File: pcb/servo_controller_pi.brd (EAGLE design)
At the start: 129 parts, among them IC1 PIC18F452, IC2 DS1307, IC3 MAX4173FESA+, IC4 LM2936MP-3.3, IC6 LM386M-1, IC7 GY-27, IC8 MCP23017SO, Q1 10Mhz, Q2 BC848ASMD, Q3 BC848ASMD

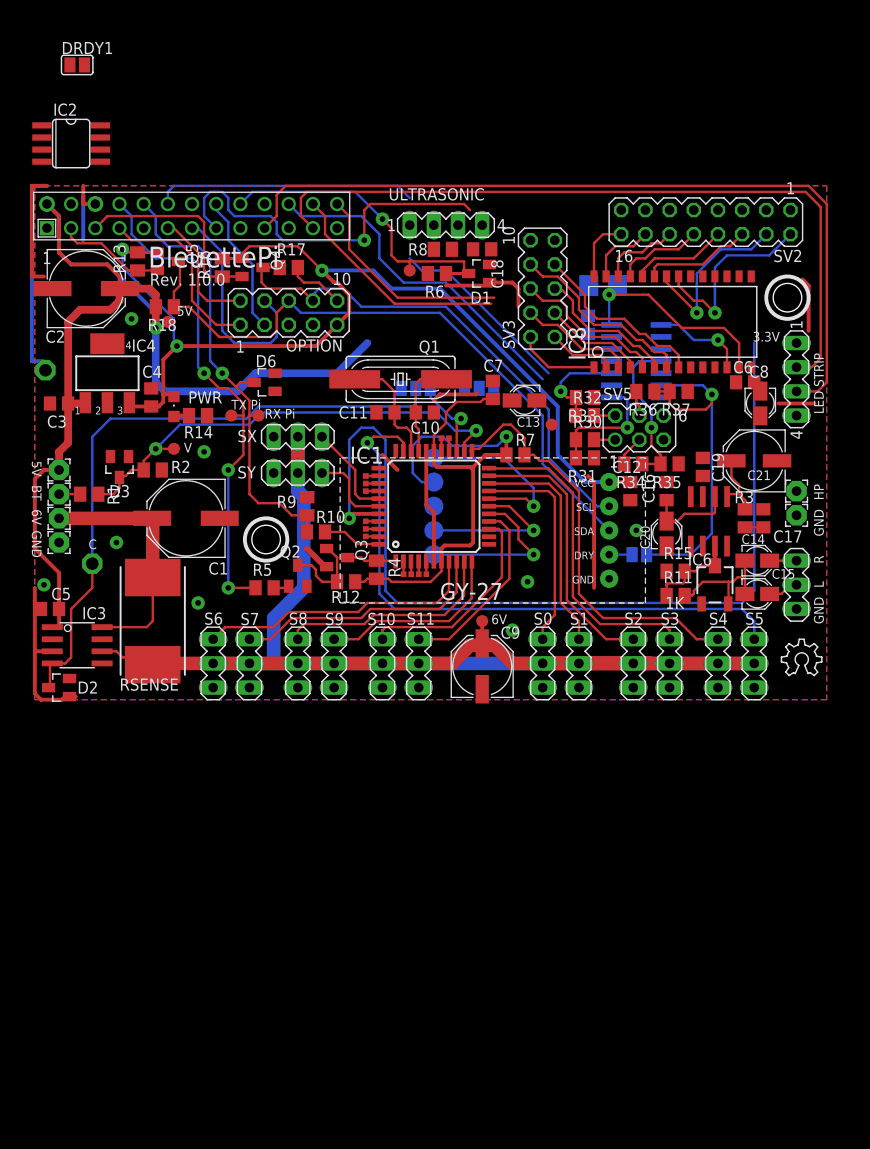
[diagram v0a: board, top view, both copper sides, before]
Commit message: BleuettePi : Add RTC Clock
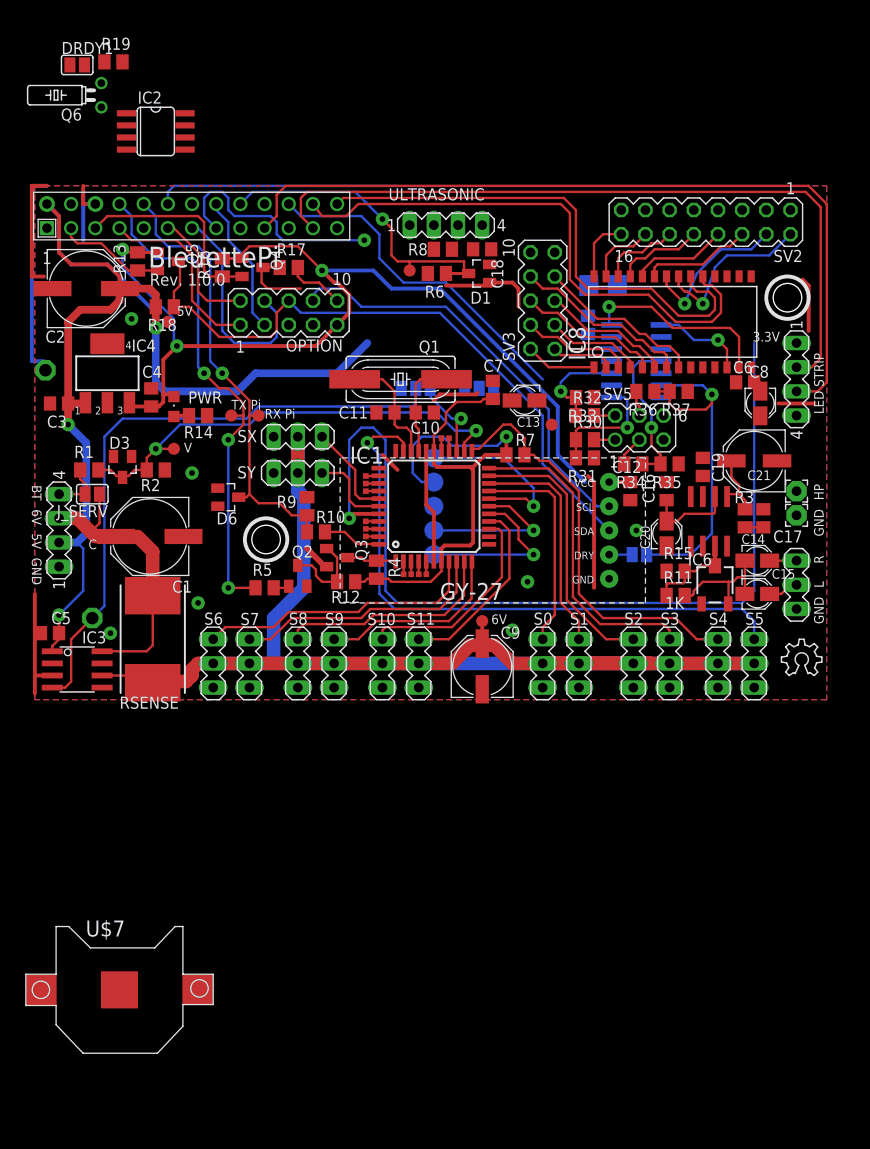
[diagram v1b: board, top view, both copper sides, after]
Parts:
- removed D2: 5V1, diode:SOT23
- removed P5V, P6V, PBATT, PGND: (no value), wirepad:2,15/1,0
- added J_SERV: (no value), jumper:SJ
- added Q6: (no value), crystal:TC26H
- added R19: 10, rcl:M0805
- added SV1: (no value), con-lstb:MA04-1
- added U$7: (no value), adafruit:CR1220-SMD
- IC2: value DS1307 -> DS1339
- Q1: device crystal:HC49UP -> crystal:HC49UP@1
- moved D6 12.7 mm to (21.6, 22.5), turned to 270 degrees
- moved IC2 8.98 mm to (14.0, 61.6)
- moved T_CURRENT 5.71 mm to (7.30, 9.84)
- moved C1 4.26 mm to (13.3, 18.4)
- moved IC3 2.54 mm to (5.71, 4.45)
- moved C5 2.54 mm to (2.86, 8.26)
- moved R1 2.54 mm to (6.99, 25.4)
- moved RSENSE 1.91 mm to (13.7, 7.62)
- moved SV3 1.27 mm to (54.6, 43.2)
- moved R2 0.32 mm to (14.0, 25.4)
- moved D3 0.32 mm to (10.5, 25.7)
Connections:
- removed net GND: IC2.4
- removed net INT1: DRDY.1, OPTION.5
- removed net VBAT: IC2.3
- removed net VCC: IC2.8
- removed net __: U$3.22
- new net INTC: IC2.7, OPTION.8, R19.1, U$3.22
- new net INTD: DRDY.1
- new net N$33: IC2.1, Q6.2
- new net N$34: IC2.2, Q6.1
- new net N$58: IC2.3, U$7.-
- net +3V3: now also R19.2, U$3.1; no longer C12.1, IC7.VCC
- net +5V: now also C12.1, IC2.8, IC7.VCC, SV1.2; no longer P5V.1
- net +7V: now also J_SERV.1, SV1.3; no longer P6V.1
- net INTA: now also U$3.26; no longer U$3.24
- net INTB: now also U$3.24; no longer U$3.26
- net SCL: now also IC2.6, OPTION.5; no longer OPTION.8
- net SDA: now also IC2.5
- net SERVO_CURRENT: no longer D2.3
- net VDD: now also J_SERV.2, SV1.4; no longer PBATT.1
- net VSS: now also IC2.4, SV1.1, U$7.+$1, U$7.+$2; no longer D2.1, PGND.1
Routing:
- net INTB: track 22.6 -> 58.6 mm
- net __: track 35.8 -> 0.00 mm
- net INTC: track 0.00 -> 35.8 mm
- net INTA: track 24.2 -> 54.7 mm
- net INTD: track 0.00 -> 21.7 mm
- net INT1: track 21.7 -> 0.00 mm
- net OUT: track 47.1 -> 25.7 mm
- net TRIGGER: track 39.2 -> 24.4 mm
- net VSS: track 115.5 -> 109.5 mm, vias 8 -> 7
- net +5V: track 195.5 -> 200.8 mm, vias 2 -> 4
- net +3V3: track 114.9 -> 110.1 mm
- net VDD: track 2.23 -> 5.66 mm
- net GPA0: track 20.1 -> 17.6 mm
- net +7V: track 28.1 -> 30.6 mm
- net SCL: track 64.0 -> 61.5 mm
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
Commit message: BleuettePi
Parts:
- added C23, C25, C26, C27, C28, C29: 100nf, rcl:C0805
- moved U$7 83.7 mm to (41.9, 48.3), flipped to the bottom
- moved R19 46.9 mm to (47.9, 41.3), turned to 270 degrees
- moved Q6 35.5 mm to (37.8, 45.1), turned to 0 degrees
- moved IC2 34.5 mm to (42.5, 42.2)
- moved T_CURRENT 16.2 mm to (18.7, 21.3)
- moved C5 11.6 mm to (14.3, 10.5), turned to 0 degrees
- moved RSENSE 8.89 mm to (4.76, 7.62)
- moved IC3 7.73 mm to (13.0, 6.99), turned to 90 degrees
- moved J_VOLT 3.59 mm to (45.4, 36.5)
- moved C24 2.56 mm to (63.2, 46.0)
- moved C1 2.01 mm to (12.7, 16.5)
- moved U$4 1.59 mm to (64.5, 38.4)
- moved C22 1.42 mm to (58.7, 41.9)
- moved SV1 1.27 mm to (3.81, 20.3)
- moved C11 0.71 mm to (37.5, 31.1), turned to 180 degrees
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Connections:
- net N$18: now also C23.1
- net N$28: now also C25.1
- net N$29: now also C26.1
- net N$30: now also C27.1
- net PIC_LIPO_VOLTAGE: now also C29.1
- net PIC_SERVO_CURRENT: now also C28.1
- net VSS: now also C23.2, C25.2, C26.2, C27.2, C28.2, C29.2
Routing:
- net SERVO_CURRENT: track 65.1 -> 43.4 mm
- net VSS: track 109.5 -> 92.3 mm, vias 7 -> 6
- net VEE: track 185.2 -> 193.6 mm
- net N$30: track 14.5 -> 18.6 mm
- net N$28: track 10.4 -> 13.3 mm
- net N$29: track 16.4 -> 19.2 mm
- net PIC_LIPO_VOLTAGE: track 0.09 -> 2.65 mm
- net +5V: track 200.8 -> 198.4 mm
- net SDA: track 88.1 -> 85.8 mm
- net INTD: track 21.7 -> 19.8 mm
- net LIPO_VOLTAGE: track 49.0 -> 47.1 mm
- net +7V: track 30.6 -> 28.7 mm
- net N$18: track 13.0 -> 14.4 mm
- net N$27: track 10.6 -> 9.81 mm
- net ECHO: track 35.2 -> 36.1 mm
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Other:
- board text added: "Isoler la partie ADC"

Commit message: BleuettePi, modif ADC
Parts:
- removed AN6, AN7, RC4, RC5, RD3, RD4, RD5, RD6, RD7: TPSQTP06SQ, testpad:TP06SQ
- removed C28, C29: 100nf, rcl:C0805
- removed DRDY1: (no value), jumper:SJ
- removed J_CURRENT, J_VOLT: (no value), jumper:SJ_2
- removed R30, R32, R34, R36: 10k 1%, rcl:M0805
- removed R31, R33, R35, R37: 6.8k 1%, rcl:M0805
- removed R7: 2.2k, rcl:M0805
- removed U$4: MCP3424-E/SL, eagleParts:SOIC-14
- C24: value 10uf -> 100nf; device rcl:CT3528 -> rcl:C0805
- SV5: device con-lstb:MA03-2 -> con-lstb:MA04-2
- moved C27 105.2 mm to (1.27, -43.2), flipped to the top, turned to 0 degrees
- moved C26 96.1 mm to (1.27, -37.1), flipped to the top, turned to 0 degrees
- moved C24 94.3 mm to (1.27, -25.1), flipped to the top, turned to 0 degrees
- moved C25 90.0 mm to (1.27, -31.1), flipped to the top, turned to 0 degrees
- moved C22 79.5 mm to (1.27, -13.0), flipped to the top, turned to 0 degrees
- moved C23 79.2 mm to (1.27, -19.1), flipped to the top
- moved SV5 69.4 mm to (4.76, -5.08)
- moved S10 35.2 mm to (73.0, 5.08)
- moved S2 35.2 mm to (28.9, 5.08)
- moved S4 35.2 mm to (37.8, 5.08)
- moved S8 35.2 mm to (64.1, 5.08)
- moved S11 35.2 mm to (76.8, 5.08)
- moved S3 35.2 mm to (32.7, 5.08)
- moved S5 35.2 mm to (41.6, 5.08)
- moved S9 35.2 mm to (67.9, 5.08)
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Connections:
- net N$10 renamed SS6
- net N$11 renamed SS7
- net N$12 renamed SS8
- net N$13 renamed SS9
- net N$14 renamed SS10
- removed net CAN0: R30.2, SV5.1
- removed net CAN1: R32.2, SV5.2
- removed net CAN2: J_CURRENT.3, R34.2, SV5.3
- removed net CAN3: J_VOLT.3, R36.2, SV5.4
- removed net INT0: IC1.40
- removed net LIPO_VOLTAGE: D3.3, J_VOLT.2, R1.1, R2.2, T_LVOLTAGE.TP
- removed net N$18: C23.1, R30.1, R31.2, U$4.1
- removed net N$2: IC1.20, S1.3
- removed net N$20: AN7.TP, IC1.27
- removed net N$26: AN6.TP, IC1.26
- removed net N$28: C25.1, R32.1, R33.2, U$4.3
- removed net N$29: C26.1, R34.1, R35.2, U$4.11
- removed net N$3: IC1.21, S2.3
- removed net N$30: C27.1, R36.1, R37.2, U$4.13
- removed net N$32: IC1.15, S11.3
- removed net N$4: IC1.22, S3.3
- removed net N$48: IC1.5, RD7.TP
- removed net N$49: IC1.4, RD6.TP
- removed net N$5: IC1.23, R7.1, S4.3
- removed net N$50: IC1.3, RD5.TP
- removed net N$51: IC1.2, RD4.TP
- removed net N$57: IC1.41, RD3.TP
- removed net N$6: IC1.32, S5.3
- removed net PIC_LIPO_VOLTAGE: C29.1, IC1.24, J_VOLT.1
- removed net PIC_SERVO_CURRENT: C28.1, IC1.25, J_CURRENT.1
- removed net SERVO_CURRENT: IC3.4, J_CURRENT.2, T_CURRENT.TP
- new net AN0: C27.2, IC1.19, SV5.1
- new net AN1: C26.2, IC1.20, SV5.2
- new net AN2: C25.2, IC1.21, SV5.3
- new net AN3: C24.2, IC1.22, SV5.4
- new net AN4: C23.2, IC1.24, SV5.5
- new net AN5: C22.2, IC1.25, SV5.6
- new net AN6: D3.3, IC1.26, R1.1, R2.2, T_LVOLTAGE.TP
- new net AN7: IC1.27, IC3.4, T_CURRENT.TP
- new net SS0: IC1.40, S0.3
- new net SS1: IC1.41, S1.3
- new net SS11: IC1.15
- new net SS2: IC1.2, S2.3
- new net SS3: IC1.3, S3.3
- new net SS4: IC1.4, S4.3
- new net SS5: IC1.5, S5.3
- net +5V: now also SV5.8; no longer C22.1, C24.+, R7.2, SV5.6, U$4.6
- net INTD: now also IC1.32
- net N$1: now also S11.3; no longer IC1.19, S0.3
- net N$55: no longer RC4.TP
- net N$56: no longer RC5.TP
- net SCL: no longer U$4.8
- net SDA: no longer U$4.7
- net VSS: now also C22.1, C23.1, C24.1, C25.1, C26.1, C27.1, SV5.7; no longer C22.2, C23.2, C24.-, C25.2, C26.2, C27.2, C28.2, C29.2, R31.1, R33.1, R35.1, R37.1, SV5.5, U$4.10, U$4.12, U$4.14, U$4.2, U$4.4, U$4.5, U$4.9
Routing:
- net VEE: track 193.6 -> 61.8 mm
- net INT0: track 98.1 -> 0.00 mm, vias 1 -> 0
- net N$6: track 64.1 -> 0.00 mm, vias 1 -> 0
- net LIPO_VOLTAGE: track 47.1 -> 0.00 mm, vias 2 -> 0
- net N$5: track 44.1 -> 0.00 mm
- net SERVO_CURRENT: track 43.4 -> 0.00 mm
- net AN4: track 0.00 -> 40.8 mm, vias 0 -> 2
- net N$4: track 33.4 -> 0.00 mm
- net SS6: track 30.0 -> 0.00 mm
- net N$3: track 28.8 -> 0.00 mm
- net SS7: track 27.0 -> 0.00 mm
- net N$2: track 23.9 -> 0.00 mm
- net SS8: track 23.5 -> 0.00 mm
- net N$1: track 22.6 -> 0.00 mm
- net SS10: track 22.1 -> 0.00 mm
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
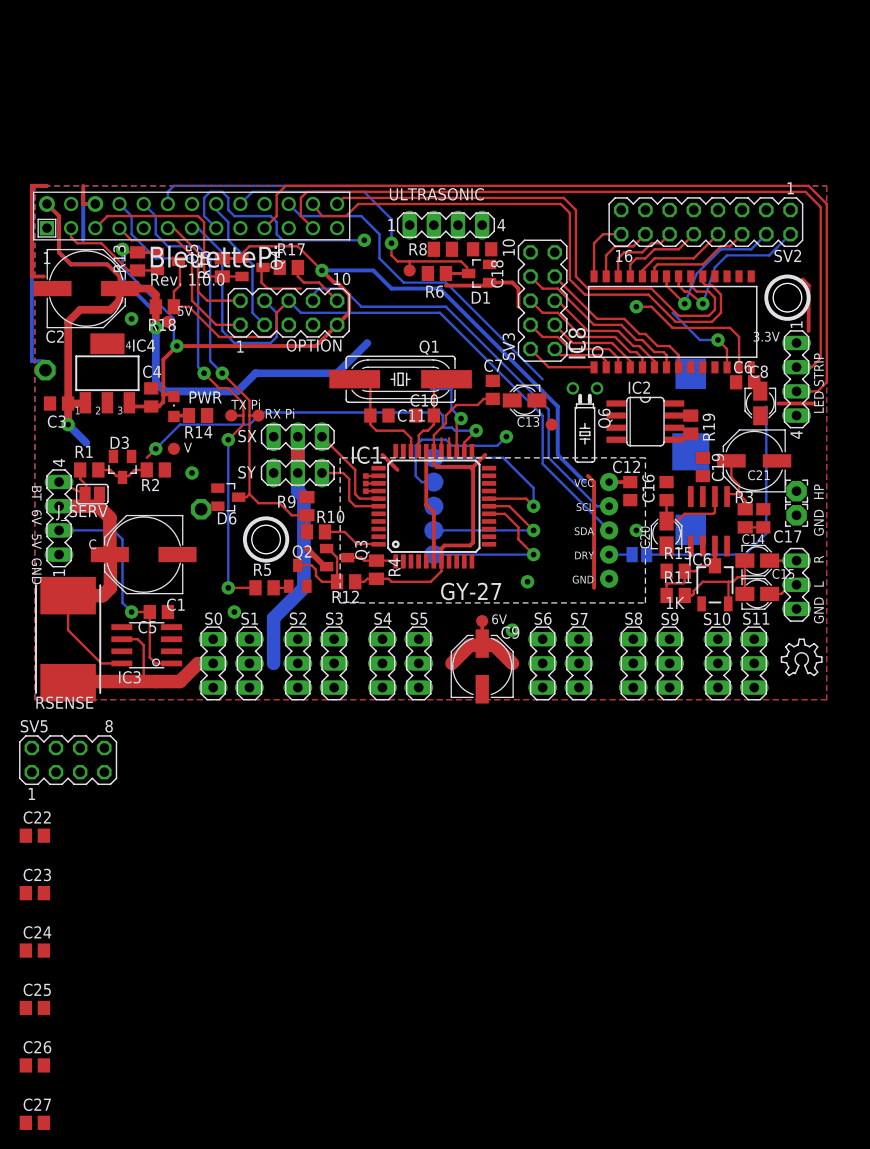
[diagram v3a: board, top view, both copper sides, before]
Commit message: BleuettePi : ADC modif
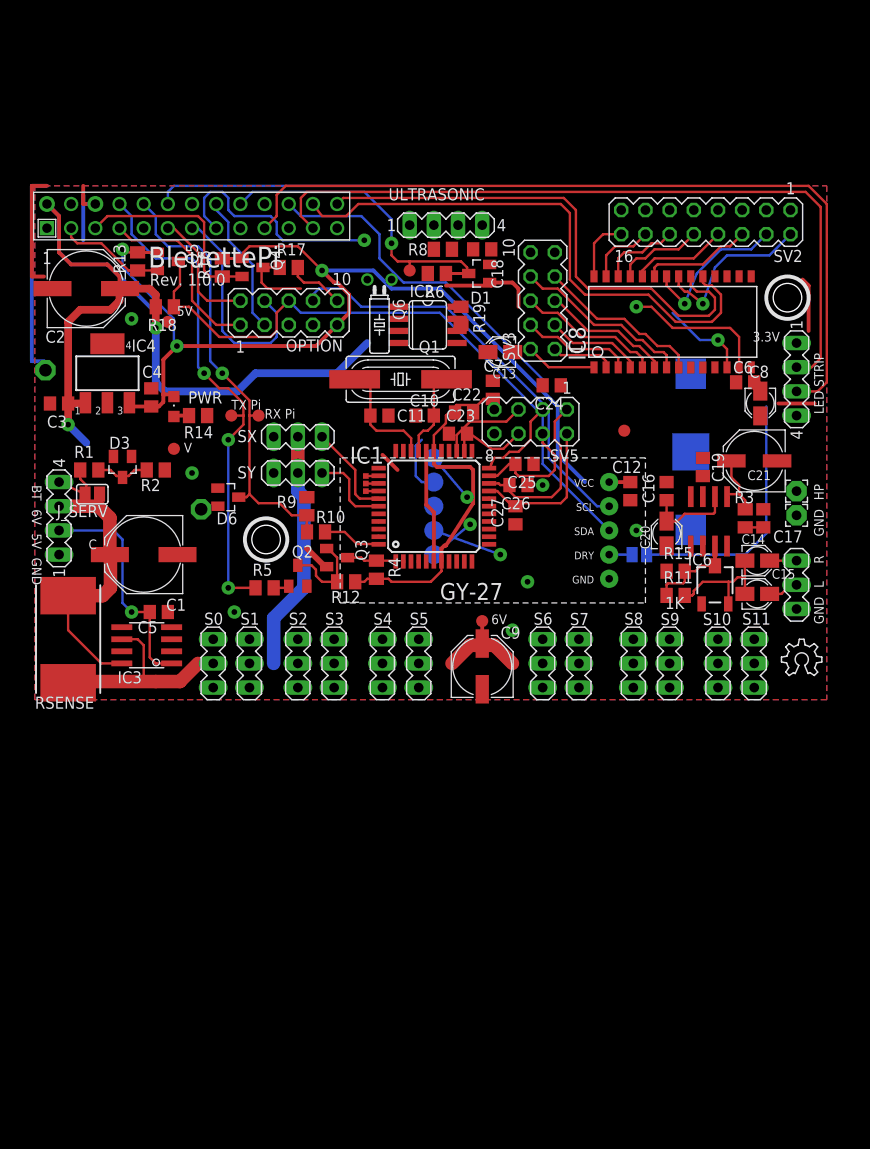
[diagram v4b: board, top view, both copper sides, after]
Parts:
- moved C27 81.4 mm to (51.8, 20.6), turned to 90 degrees
- moved C24 80.5 mm to (55.6, 34.3), turned to 180 degrees
- moved C26 79.4 mm to (52.1, 23.8), turned to 180 degrees
- moved C25 76.9 mm to (52.7, 26.0), turned to 180 degrees
- moved C23 65.6 mm to (45.7, 29.2)
- moved C22 63.3 mm to (46.4, 31.4)
- moved SV5 60.2 mm to (53.3, 30.5), turned to 180 degrees
- moved R19 26.7 mm to (46.0, 41.6)
- moved IC2 25.0 mm to (42.5, 41.3)
- moved Q6 24.4 mm to (37.5, 45.4)
- moved T_3.3V 7.65 mm to (63.2, 29.5)
- moved C13 5.68 mm to (50.2, 37.8)
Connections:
- net AN0: now also SV5.2; no longer SV5.1
- net AN1: now also SV5.1; no longer SV5.2
- net AN2: now also SV5.4; no longer SV5.3
- net AN3: now also SV5.3; no longer SV5.4
- net AN4: now also SV5.6; no longer SV5.5
- net AN5: now also SV5.5; no longer SV5.6
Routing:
- net AN4: track 40.8 -> 8.35 mm, vias 2 -> 0
- net AN1: track 0.00 -> 17.9 mm
- net AN0: track 0.00 -> 15.6 mm
- net +5V: track 194.3 -> 180.9 mm, vias 4 -> 3
- net UC_RESET: track 18.7 -> 5.48 mm
- net AN2: track 0.00 -> 13.1 mm
- net N$23: track 17.7 -> 4.96 mm
- net VSS: track 92.3 -> 80.3 mm, vias 6 -> 7
- net AN3: track 0.00 -> 9.58 mm
- net N$22: track 16.2 -> 7.43 mm
- net AN7: track 1.34 -> 0.00 mm
- net AN6: track 7.18 -> 5.84 mm
- net AN5: track 9.29 -> 9.28 mm, vias 1 -> 0

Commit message: BleuettePi work !
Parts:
- removed D6: 3V3, diode:SOT23
- removed R5: 470, rcl:M0805
- added C28, C29: 100nf, rcl:C0805
- Q2, Q3: value BC848ASMD -> (none); device transistor-npn:SOT23 -> adafruit:SOT23
- moved T_3.3V 28.2 mm to (37.1, 40.3)
- moved Q6 26.9 mm to (61.0, 32.4)
- moved IC2 26.8 mm to (67.3, 31.1)
- moved SX 16.8 mm to (17.1, 16.8), turned to 270 degrees
- moved Q3 16.5 mm to (26.7, 31.4)
- moved RESET 15.8 mm to (51.1, 13.0)
- moved R19 14.2 mm to (33.0, 47.3), turned to 180 degrees
- moved R4 14.0 mm to (28.6, 26.0), turned to 90 degrees
- moved R12 13.9 mm to (23.8, 23.2), turned to 90 degrees
- moved VDD 12.4 mm to (48.6, 13.0)
- moved R9 11.7 mm to (23.5, 31.4), turned to 90 degrees
- moved SY 11.5 mm to (21.0, 16.8), turned to 270 degrees
- moved C24 10.8 mm to (49.8, 25.1), turned to 270 degrees
- moved R10 10.8 mm to (26.7, 28.9), turned to 180 degrees
- moved Q2 9.16 mm to (26.7, 23.2), turned to 270 degrees
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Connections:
- removed net N$1: S11.3
- removed net N$21: Q2.3, Q3.1, R12.1
- removed net N$44: Q2.1, R5.2
- new net AGND: C22.1, C23.1, C24.1, C25.1, C26.1, C27.1, C28.1, C29.1, SV5.7
- net +3V3: now also Q2.1, Q3.1, R12.2, R9.2
- net +5V: now also R10.2; no longer R12.2
- net AN6: now also C28.2
- net AN7: now also C29.2
- net N$16: now also Q3.3, R10.1; no longer R10.2
- net N$33: now also Q6.1; no longer Q6.2
- net N$34: now also Q6.2; no longer Q6.1
- net RX_PI: now also Q3.2, R9.1; no longer D6.3, R10.1, R9.2
- net RX_PIC: now also Q2.3; no longer Q3.3
- net SS11: now also S11.3
- net TX_PI: now also Q2.2, R12.1; no longer R5.1
- net VSS: no longer C22.1, C23.1, C24.1, C25.1, C26.1, C27.1, D6.1, Q2.2, Q3.2, R9.1, SV5.7
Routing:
- net +5V: track 180.9 -> 306.3 mm, vias 3 -> 7
- net VEE: track 61.8 -> 172.1 mm, vias 0 -> 1
- net AGND: track 0.00 -> 93.6 mm, vias 0 -> 2
- net AN7: track 0.00 -> 46.5 mm, vias 0 -> 2
- net AN6: track 5.84 -> 44.1 mm, vias 0 -> 2
- net SS11: track 0.00 -> 35.6 mm
- net INTC: track 35.8 -> 67.4 mm, vias 0 -> 1
- net SS10: track 0.00 -> 31.5 mm
- net SCL: track 60.8 -> 88.3 mm, vias 1 -> 3
- net INTD: track 26.8 -> 0.00 mm
- net SS9: track 0.00 -> 25.7 mm
- net SS8: track 0.00 -> 23.0 mm
- net SS0: track 0.00 -> 21.1 mm, vias 0 -> 1
- net SS7: track 0.00 -> 18.5 mm
- net SDA: track 83.6 -> 101.8 mm, vias 1 -> 2
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- added copper zone on layer 1, net AGND
- added copper zone on layer 16, net AGND
